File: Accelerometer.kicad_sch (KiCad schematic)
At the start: 0 parts

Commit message: top-level structure and ESP32-C6 pin assignments nearly sorted
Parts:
- added C3, C4: 100n, Capacitor_SMD:C_0603_1608Metric, symbol Device:C
- added C5: 10u, Capacitor_SMD:C_0603_1608Metric, symbol Device:C
- added U5: LIS2DH12TR, Package_LGA:LGA-14_2x2mm_P0.35mm_LayoutBorder3x4y, symbol Sensor_Motion:LIS2DH
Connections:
- new net GND: C3.2, C4.2, C5.2, U5.10 (GND), U5.11 (GND), U5.12 (GND), U5.13 (GND), U5.14 (GND), U5.3 (SDO), U5.9 (GND)
- new net SCL: U5.1 (SCL/SPC)
- new net SDA: U5.2 (SDA/SDI)
- new net VDD: C3.1, C4.1, C5.1, U5.7 (Vdd_IO), U5.8 (Vdd)
- no-connect marks 0 -> 2
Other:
- note added: "I2C address = 0x18"
- company: (none) -> Sunrise designs
- title: (none) -> Open polysomnography board

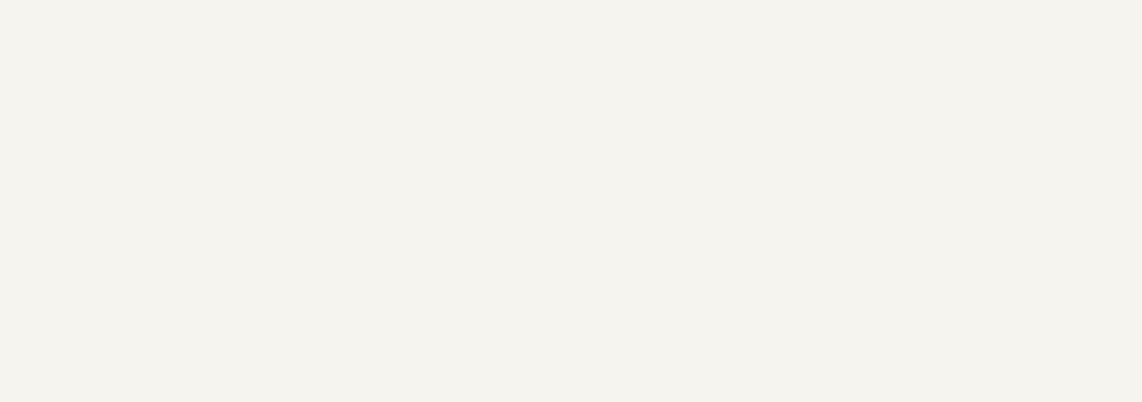
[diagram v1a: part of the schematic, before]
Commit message: text comments sections added
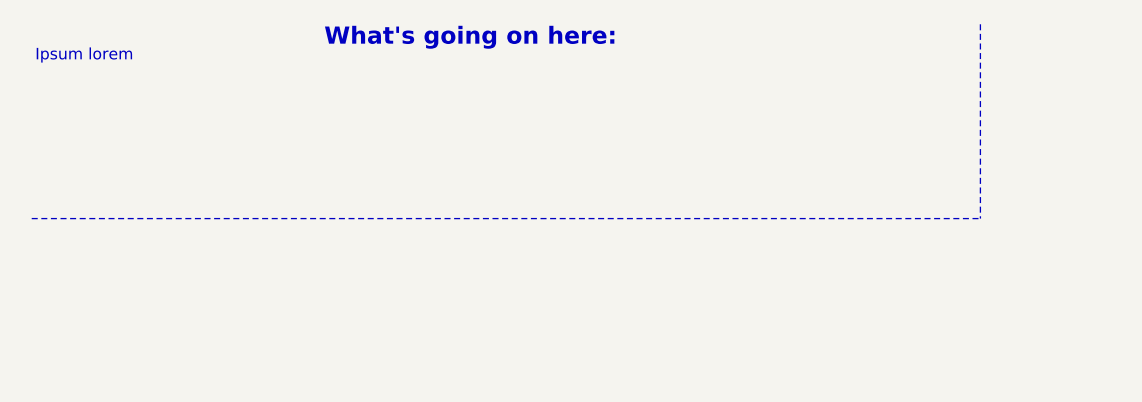
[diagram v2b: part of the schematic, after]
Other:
- note added: "Ipsum lorem"
- note added: "What's going on here:"
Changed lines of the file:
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@@
 		(company "Sunrise designs")
+	)
+	(text "What's going on here:\n"
+		(exclude_from_sim no)
+		(at 61.468 14.224 0)
+		(effects
+			(font
+				(size 1.905 1.905)
+				(thickness 0.381)
+				(bold yes)
+				(color 132 0 0 1)
+			)
+		)
+	)
+	(text "Ipsum lorem\n"
+		(exclude_from_sim no)
+		(at 18.542 16.256 0)
+		(effects
+			(font
+				(size 1.27 1.27)
+				(color 132 0 0 1)
+			)
+		)
 	)
 	(text "I2C address = 0x18"
@@
 		)
 	)
+	(polyline
+		(pts
+			(xy 12.7 34.29) (xy 118.11 34.29)
+		)
+		(stroke
+			(width 0)
+			(type dash)
+			(color 132 0 0 1)
+		)
+	)
 	(wire
 		(pts
@@
 		)
 	)
+	(polyline
+		(pts
+			(xy 118.11 12.7) (xy 118.11 34.29)
+		)
+		(stroke
+			(width 0)
+			(type dash)
+			(color 132 0 0 1)
+		)
+	)
